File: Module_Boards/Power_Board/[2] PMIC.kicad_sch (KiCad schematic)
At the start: 24 parts, among them U2 MAX77654MENV+T

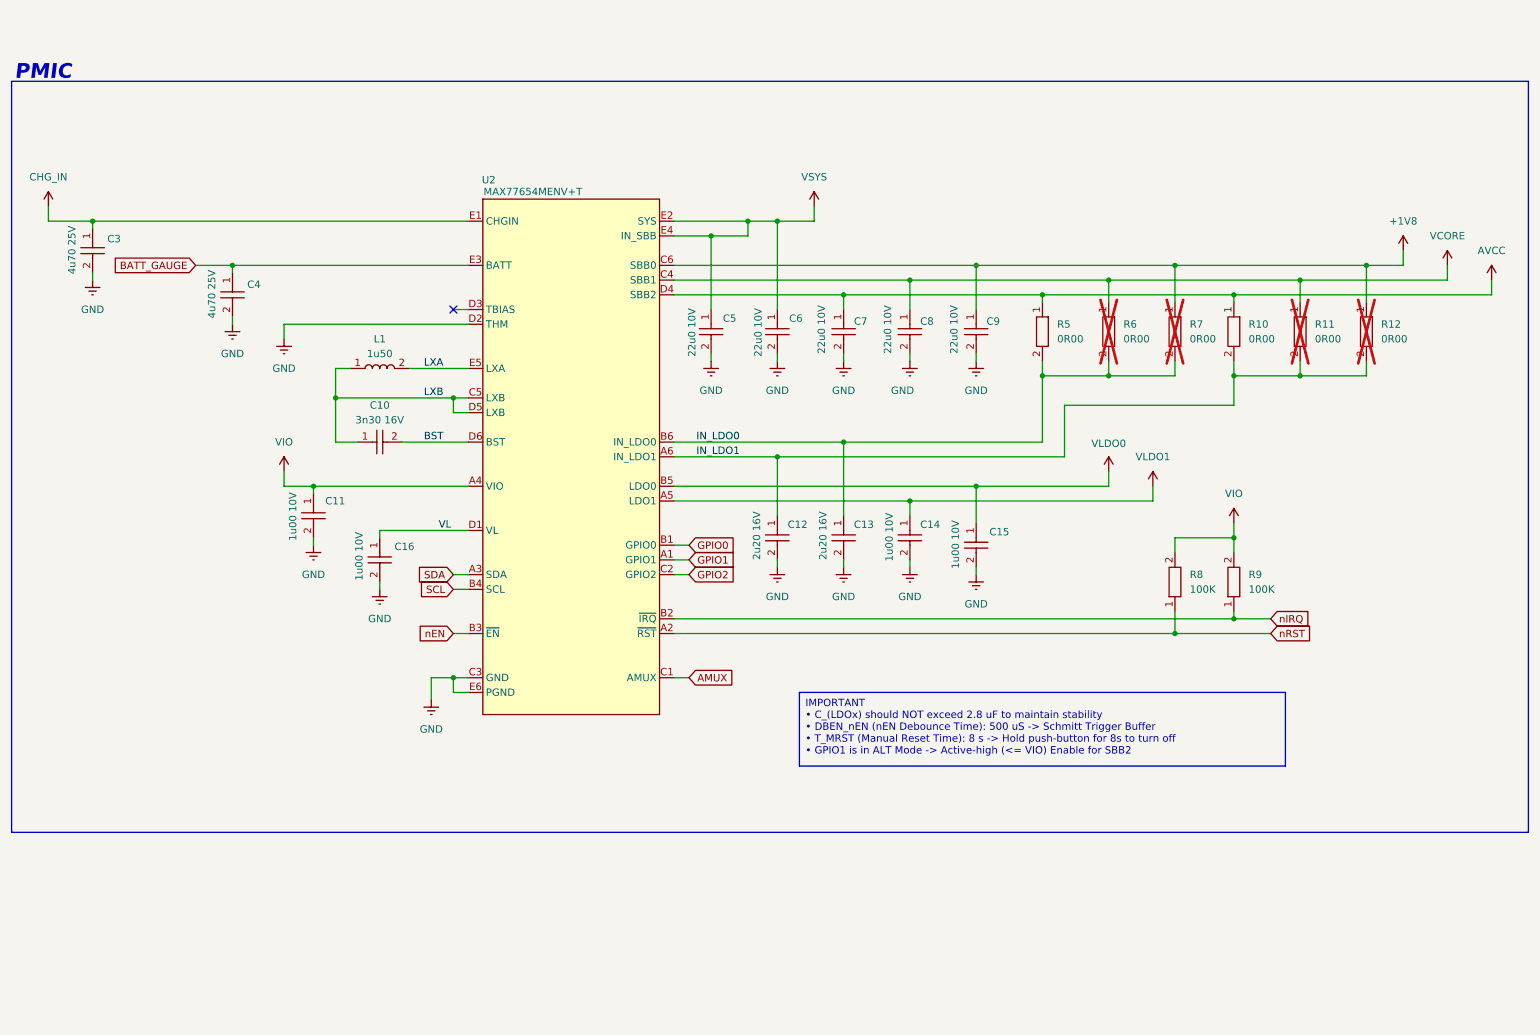
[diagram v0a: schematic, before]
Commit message: Fixed bugs. Added comments. Push before changing the ADC
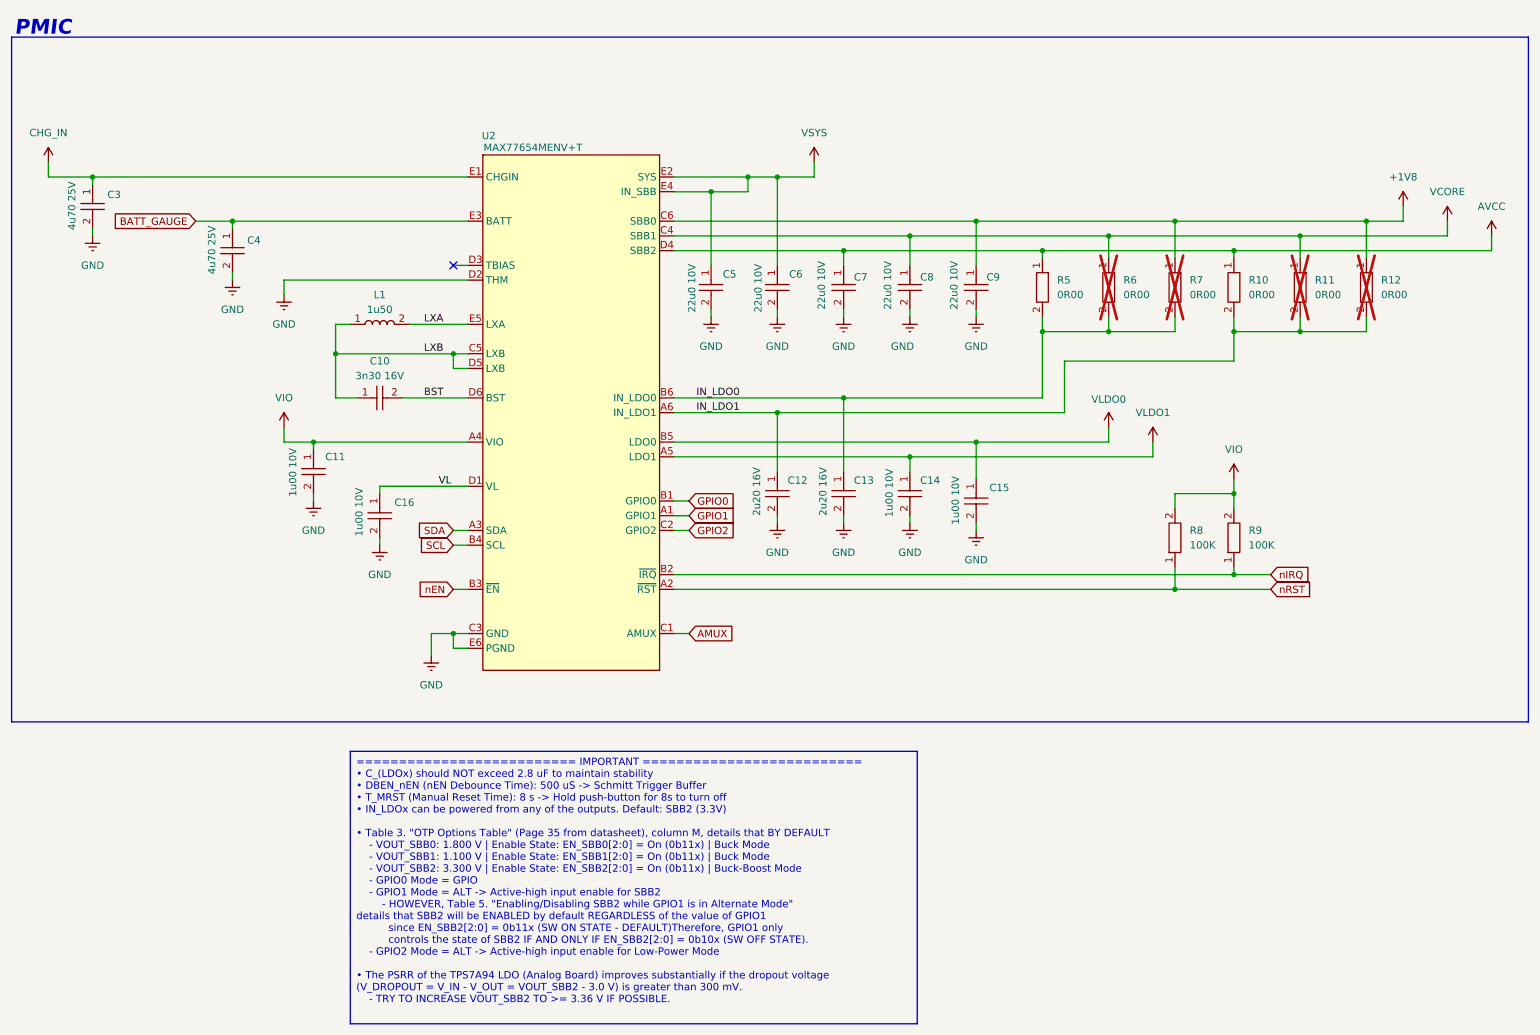
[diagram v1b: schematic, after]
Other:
- moved on the sheet: C10, C11, C12, C13, C14, C15, C16, C3, C4, C5, C6, C7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

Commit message: Push with updated readme
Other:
- moved on the sheet: C10, C11, C12, C13, C14, C15, C16, C3, C4, C5, C6, C7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
